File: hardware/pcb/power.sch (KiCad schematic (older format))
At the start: 15 parts

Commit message: schematic updates
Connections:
- net GND: no longer C?.2 (BATT-)
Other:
- moved on the sheet: C?, U?
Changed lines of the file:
@@
 L TPS783 U?
 U 1 1 552EDEA7
-P 5500 5700
-F 0 "U?" H 5350 5950 60  0000 C CNN
-F 1 "TPS783" H 5650 5450 60  0000 C CNN
-F 2 "" H 5350 5650 60  0000 C CNN
-F 3 "" H 5350 5650 60  0000 C CNN
-	1    5500 5700
-	1    0    0    -1
-$EndComp
-Text HLabel 6500 5600 2    60   Input ~ 0
+P 6500 4100
+F 0 "U?" H 6350 4350 60  0000 C CNN
+F 1 "TPS783" H 6650 3850 60  0000 C CNN
+F 2 "" H 6350 4050 60  0000 C CNN
+F 3 "" H 6350 4050 60  0000 C CNN
+	1    6500 4100
+	1    0    0    -1
+$EndComp
+Text HLabel 7500 3550 1    60   Input ~ 0
 +3V
 $Comp
 L GND #PWR035
 U 1 1 552EE044
-P 5500 6200
-F 0 "#PWR035" H 5500 5950 50  0001 C CNN
-F 1 "GND" H 5500 6050 50  0000 C CNN
-F 2 "" H 5500 6200 60  0000 C CNN
-F 3 "" H 5500 6200 60  0000 C CNN
-	1    5500 6200
+P 6500 4600
+F 0 "#PWR035" H 6500 4350 50  0001 C CNN
+F 1 "GND" H 6500 4450 50  0000 C CNN
+F 2 "" H 6500 4600 60  0000 C CNN
+F 3 "" H 6500 4600 60  0000 C CNN
+	1    6500 4600
 	1    0    0    -1
 $EndComp
@@
 L C C?
 U 1 1 552EE08E
-P 4850 5750
-F 0 "C?" H 4875 5850 50  0000 L CNN
-F 1 "C" H 4875 5650 50  0000 L CNN
-F 2 "" H 4888 5600 30  0000 C CNN
-F 3 "" H 4850 5750 60  0000 C CNN
-	1    4850 5750
+P 5850 4150
+F 0 "C?" H 5875 4250 50  0000 L CNN
+F 1 "C" H 5875 4050 50  0000 L CNN
+F 2 "" H 5888 4000 30  0000 C CNN
+F 3 "" H 5850 4150 60  0000 C CNN
+	1    5850 4150
 	1    0    0    -1
 $EndComp
@@
 L C C?
 U 1 1 552EE0AE
-P 6100 5750
-F 0 "C?" H 6125 5850 50  0000 L CNN
-F 1 "C" H 6125 5650 50  0000 L CNN
-F 2 "" H 6138 5600 30  0000 C CNN
-F 3 "" H 6100 5750 60  0000 C CNN
-	1    6100 5750
+P 7100 4150
+F 0 "C?" H 7125 4250 50  0000 L CNN
+F 1 "C" H 7125 4050 50  0000 L CNN
+F 2 "" H 7138 4000 30  0000 C CNN
+F 3 "" H 7100 4150 60  0000 C CNN
+	1    7100 4150
 	1    0    0    -1
 $EndComp
@@
 $EndComp
 Wire Wire Line
-	5500 6100 5500 6200
-Connection ~ 5500 6100
-Wire Wire Line
-	4850 5600 5050 5600
-Wire Wire Line
-	5050 5700 5000 5700
-Wire Wire Line
-	5000 5700 5000 6100
-Wire Wire Line
-	5000 6100 5900 6100
-Wire Wire Line
-	5900 5600 6500 5600
-Connection ~ 6100 5600
-Wire Wire Line
-	5900 6100 5900 5700
-Wire Wire Line
-	6100 5900 5900 5900
-Connection ~ 5900 5900
-Wire Wire Line
-	4850 5900 5000 5900
-Connection ~ 5000 5900
+	6500 4500 6500 4600
+Connection ~ 6500 4500
+Wire Wire Line
+	4050 4000 6050 4000
+Wire Wire Line
+	6050 4100 6000 4100
+Wire Wire Line
+	6000 4100 6000 4500
+Wire Wire Line
+	6000 4500 6900 4500
+Wire Wire Line
+	6900 4000 7500 4000
+Connection ~ 7100 4000
+Wire Wire Line
+	6900 4500 6900 4100
+Wire Wire Line
+	7100 4300 6900 4300
+Connection ~ 6900 4300
+Wire Wire Line
+	5850 4300 6000 4300
+Connection ~ 6000 4300
 Wire Wire Line
 	2350 2650 3050 2650
@@
 L LiPoly_Conn C?
 U 1 1 5530053E
-P 5750 4200
-F 0 "C?" H 5700 4600 60  0000 C CNN
-F 1 "LiPoly_Conn" H 5900 4100 60  0000 C CNN
-F 2 "" H 5750 4200 60  0000 C CNN
-F 3 "" H 5750 4200 60  0000 C CNN
-	1    5750 4200
-	1    0    0    -1
+P 5050 4550
+F 0 "C?" H 5000 4950 60  0000 C CNN
+F 1 "LiPoly_Conn" H 5200 4450 60  0000 C CNN
+F 2 "" H 5050 4550 60  0000 C CNN
+F 3 "" H 5050 4550 60  0000 C CNN
+	1    5050 4550
+	0    1    1    0
 $EndComp
 $Comp
@@
 	4050 4100 4100 4100
 $Comp
-L GND #PWR039
-U 1 1 553009E7
-P 5450 4600
-F 0 "#PWR039" H 5450 4350 50  0001 C CNN
-F 1 "GND" H 5450 4450 50  0000 C CNN
-F 2 "" H 5450 4600 60  0000 C CNN
-F 3 "" H 5450 4600 60  0000 C CNN
-	1    5450 4600
-	1    0    0    -1
-$EndComp
-Wire Wire Line
-	5450 4600 5450 4100
-Wire Wire Line
-	5450 4100 4400 4100
-Wire Wire Line
-	5550 4150 5450 4150
-Connection ~ 5450 4150
-Wire Wire Line
-	5550 4000 4050 4000
-$Comp
 L +VBATT P?
 U 1 1 55300EB5
-P 4950 3750
-F 0 "P?" H 5050 3750 60  0001 C CNN
-F 1 "+VBATT" H 4950 4050 60  0000 C CNN
-F 2 "" H 4950 3750 60  0000 C CNN
-F 3 "" H 4950 3750 60  0000 C CNN
-	1    4950 3750
-	1    0    0    -1
-$EndComp
-Wire Wire Line
-	4950 3750 4950 4000
-Connection ~ 4950 4000
-Wire Wire Line
-	4850 5600 4850 4000
+P 5550 3650
+F 0 "P?" H 5650 3650 60  0001 C CNN
+F 1 "+VBATT" H 5550 3950 60  0000 C CNN
+F 2 "" H 5550 3650 60  0000 C CNN
+F 3 "" H 5550 3650 60  0000 C CNN
+	1    5550 3650
+	1    0    0    -1
+$EndComp
 Connection ~ 4850 4000
 Text Notes 2950 4850 0    60   ~ 0
@@
 Wire Wire Line
 	4700 4200 4700 1800
+$Comp
+L GND #PWR?
+U 1 1 5539487A
+P 4550 4350
+F 0 "#PWR?" H 4550 4100 50  0001 C CNN
+F 1 "GND" H 4550 4200 50  0000 C CNN
+F 2 "" H 4550 4350 60  0000 C CNN
+F 3 "" H 4550 4350 60  0000 C CNN
+	1    4550 4350
+	1    0    0    -1
+$EndComp
+Wire Wire Line
+	4400 4100 4550 4100
+Wire Wire Line
+	4550 4100 4550 4350
+Wire Wire Line
+	5250 4350 5250 4000
+Connection ~ 5250 4000
+Wire Wire Line
+	5550 4000 5550 3650
+Connection ~ 5550 4000
+Connection ~ 5850 4000
+Wire Wire Line
+	7500 4000 7500 3550
 $EndSCHEMATC

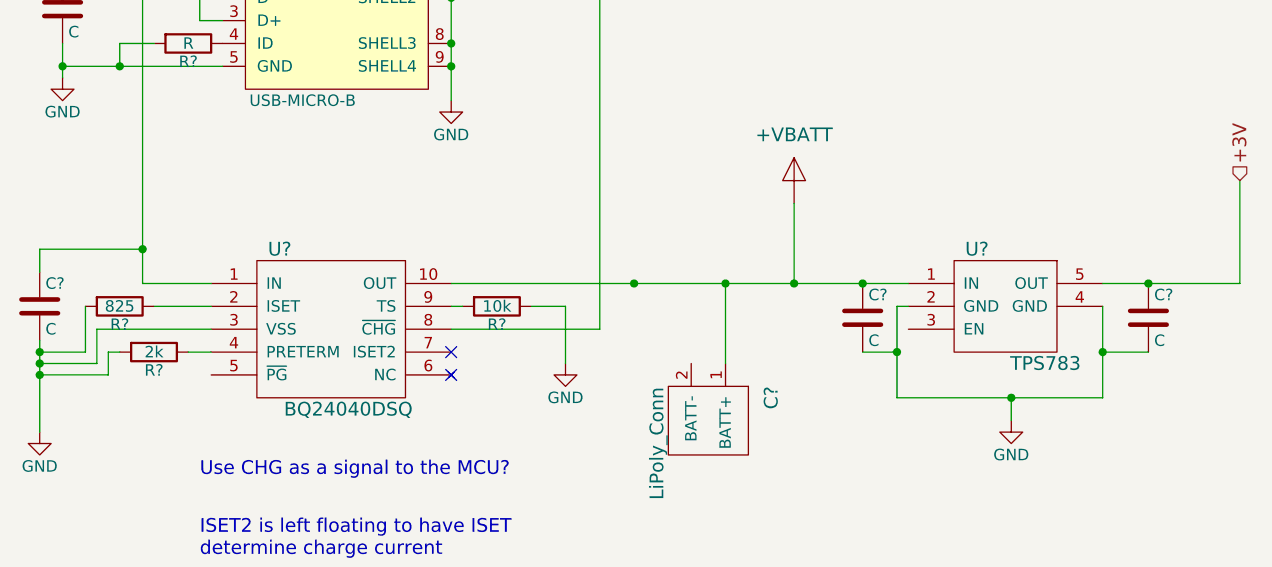
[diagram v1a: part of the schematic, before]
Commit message: Added component values
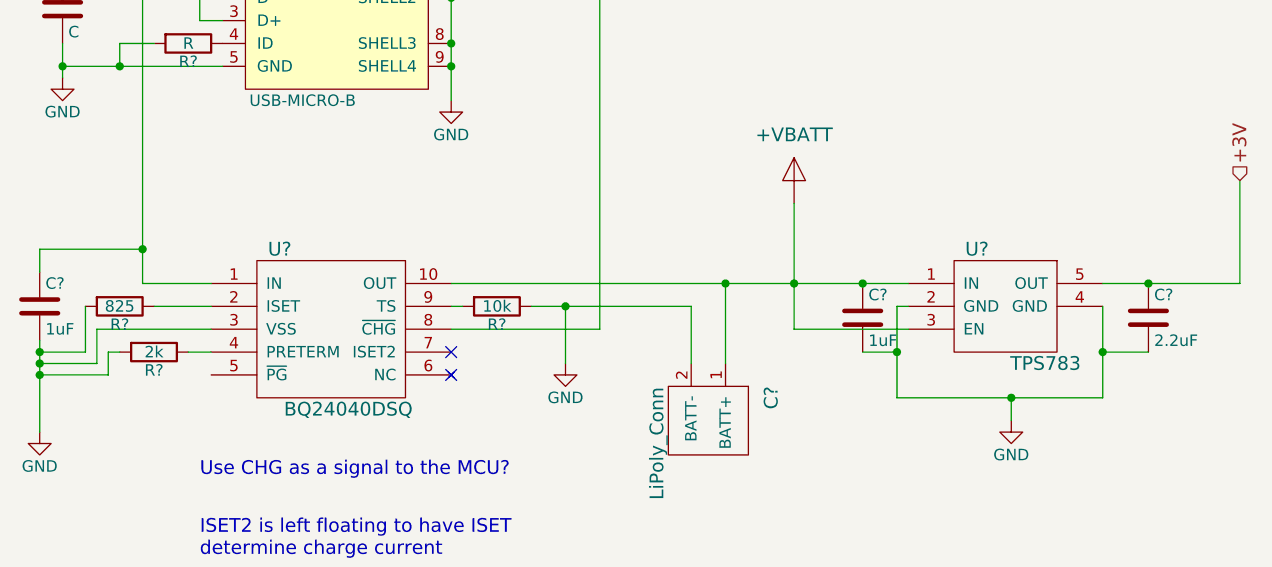
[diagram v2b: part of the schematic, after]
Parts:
- C? (x2): value C -> 1uF
- C?: value C -> 2.2uF
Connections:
- net GND: now also C?.2 (BATT-)
- net Vbatt: now also U?.3 (EN)
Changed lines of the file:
@@
 P 5850 4150
 F 0 "C?" H 5875 4250 50  0000 L CNN
-F 1 "C" H 5875 4050 50  0000 L CNN
+F 1 "1uF" H 5875 4050 50  0000 L CNN
 F 2 "" H 5888 4000 30  0000 C CNN
 F 3 "" H 5850 4150 60  0000 C CNN
@@
 P 7100 4150
 F 0 "C?" H 7125 4250 50  0000 L CNN
-F 1 "C" H 7125 4050 50  0000 L CNN
+F 1 "2.2uF" H 7125 4050 50  0000 L CNN
 F 2 "" H 7138 4000 30  0000 C CNN
 F 3 "" H 7100 4150 60  0000 C CNN
@@
 P 2250 4100
 F 0 "C?" H 2275 4200 50  0000 L CNN
-F 1 "C" H 2275 4000 50  0000 L CNN
+F 1 "1uF" H 2275 4000 50  0000 L CNN
 F 2 "" H 2288 3950 30  0000 C CNN
 F 3 "" H 2250 4100 60  0000 C CNN
@@
 	1    0    0    -1
 $EndComp
-Connection ~ 4850 4000
 Text Notes 2950 4850 0    60   ~ 0
 Use CHG as a signal to the MCU?
@@
 $EndComp
 Wire Wire Line
-	4400 4100 4550 4100
+	4400 4100 5100 4100
 Wire Wire Line
 	4550 4100 4550 4350
@@
 Connection ~ 5250 4000
 Wire Wire Line
-	5550 4000 5550 3650
+	5550 3650 5550 4200
 Connection ~ 5550 4000
 Connection ~ 5850 4000
 Wire Wire Line
 	7500 4000 7500 3550
+Wire Wire Line
+	5100 4100 5100 4350
+Connection ~ 4550 4100
+Wire Wire Line
+	5550 4200 6050 4200
 $EndSCHEMATC

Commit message: more changes
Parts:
- removed R?: R, symbol R
- gave numbers to parts that had none: 13
- renumbered 1uF to U8
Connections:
- net GND: now also CON1.4 (ID)
- net ~PG: now reaches U9.5 (~PG)

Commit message: mega commit
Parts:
- removed P1: +VBATT, symbol +VBATT
- added JP1, JP2: JUMPER, aero:Pin_Header_1x02, symbol JUMPER
- C28: renamed from C26; footprint (none) -> Capacitors_SMD:C_0603
- C29: renamed from U8; value C -> 1uF; footprint (none) -> Capacitors_SMD:C_0603
- C30: renamed from C28; footprint (none) -> Capacitors_SMD:C_0603
- C31: renamed from C29; footprint (none) -> Capacitors_SMD:C_0603
- CON1: footprint (none) -> aero:WM1399CT-ND
- J2: renamed from C27; footprint (none) -> Capacitors_SMD:C_1206_HandSoldering
- R10: renamed from R9; footprint (none) -> Resistors_SMD:R_0603
- R11: renamed from R10; footprint (none) -> Resistors_SMD:R_0603
- R7: renamed from R6; footprint (none) -> Resistors_SMD:R_0603
- R8: renamed from R7; footprint (none) -> Resistors_SMD:R_0603
- R9: renamed from R8; footprint (none) -> Resistors_SMD:R_0603
- U6: renamed from U9; footprint (none) -> aero:WSON-10-1EP
- U7: renamed from U10; footprint (none) -> Housings_SOT-23_SOT-143_TSOT-6:SOT-23-5
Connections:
- net Vbatt: now also JP2.1; no longer J2.1 (BATT+)
- net at C29.1, CON1.1 (VBUS): now also JP1.1; no longer C28.1, U6.1 (IN)
- new net: C28.1, JP1.2, U6.1 (IN)
- new net: J2.1 (BATT+), JP2.2
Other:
- moved on the sheet: C30, J2

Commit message: pre major restructuring commit
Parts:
- C25: renamed from C28; footprint Capacitors_SMD:C_0603 -> Capacitors_SMD:C_0402
- C26: renamed from C29; footprint Capacitors_SMD:C_0603 -> Capacitors_SMD:C_0402
- C27: renamed from C30; footprint Capacitors_SMD:C_0603 -> Capacitors_SMD:C_0402
- C28: renamed from C31; footprint Capacitors_SMD:C_0603 -> Capacitors_SMD:C_0402
- CON1: footprint aero:WM1399CT-ND -> (none)
- J2: footprint Capacitors_SMD:C_1206_HandSoldering -> (none)
- JP1, JP2: footprint aero:Pin_Header_1x02 -> (none)
- R10: renamed from R11; footprint Resistors_SMD:R_0603 -> Resistors_SMD:R_0402
- R6: renamed from R7; footprint Resistors_SMD:R_0603 -> Resistors_SMD:R_0402
- R7: renamed from R8; footprint Resistors_SMD:R_0603 -> Resistors_SMD:R_0402
- R8: renamed from R9; footprint Resistors_SMD:R_0603 -> Resistors_SMD:R_0402
- R9: renamed from R10; footprint Resistors_SMD:R_0603 -> Resistors_SMD:R_0402
- renumbered U6 to U7, U7 to U8
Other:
- note removed: "Use CHG as a signal to the MCU?"
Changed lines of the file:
@@
 $Descr A4 11693 8268
 encoding utf-8
-Sheet 6 7
+Sheet 6 8
 Title ""
 Date ""
@@
 $EndDescr
 $Comp
-L BQ24040DSQ U6
+L BQ24040DSQ U7
 U 1 1 552EDAA5
 P 3550 4400
-F 0 "U6" H 3300 4950 60  0000 C CNN
+F 0 "U7" H 3300 4950 60  0000 C CNN
 F 1 "BQ24040DSQ" H 3600 4250 60  0000 C CNN
 F 2 "aero:WSON-10-1EP" H 3400 4400 60  0001 C CNN
@@
 $EndComp
 $Comp
-L TPS783 U7
+L TPS783 U8
 U 1 1 552EDEA7
 P 6500 4100
-F 0 "U7" H 6350 4350 60  0000 C CNN
+F 0 "U8" H 6350 4350 60  0000 C CNN
 F 1 "TPS783" H 6650 3850 60  0000 C CNN
 F 2 "Housings_SOT-23_SOT-143_TSOT-6:SOT-23-5" H 6350 4050 60  0001 C CNN
@@
 +3V
 $Comp
-L GND #PWR043
+L GND #PWR039
 U 1 1 552EE044
 P 6500 4600
-F 0 "#PWR043" H 6500 4350 50  0001 C CNN
+F 0 "#PWR039" H 6500 4350 50  0001 C CNN
 F 1 "GND" H 6500 4450 50  0000 C CNN
 F 2 "" H 6500 4600 60  0000 C CNN
@@
 $EndComp
 $Comp
-L C C30
+L C C27
 U 1 1 552EE08E
 P 5750 4300
-F 0 "C30" H 5775 4400 50  0000 L CNN
+F 0 "C27" H 5775 4400 50  0000 L CNN
 F 1 "1uF" H 5775 4200 50  0000 L CNN
-F 2 "Capacitors_SMD:C_0603" H 5788 4150 30  0001 C CNN
+F 2 "Capacitors_SMD:C_0402" H 5788 4150 30  0001 C CNN
 F 3 "" H 5750 4300 60  0000 C CNN
 	1    5750 4300
@@
 $EndComp
 $Comp
-L C C31
+L C C28
 U 1 1 552EE0AE
 P 7100 4150
-F 0 "C31" H 7125 4250 50  0000 L CNN
+F 0 "C28" H 7125 4250 50  0000 L CNN
 F 1 "2.2uF" H 7125 4050 50  0000 L CNN
-F 2 "Capacitors_SMD:C_0603" H 7138 4000 30  0001 C CNN
+F 2 "Capacitors_SMD:C_0402" H 7138 4000 30  0001 C CNN
 F 3 "" H 7100 4150 60  0000 C CNN
 	1    7100 4150
@@
 $EndComp
 $Comp
-L C C29
+L C C26
 U 1 1 552EE372
 P 2350 2800
-F 0 "C29" H 2375 2900 50  0000 L CNN
+F 0 "C26" H 2375 2900 50  0000 L CNN
 F 1 "1uF" H 2375 2700 50  0000 L CNN
-F 2 "Capacitors_SMD:C_0603" H 2388 2650 30  0001 C CNN
+F 2 "Capacitors_SMD:C_0402" H 2388 2650 30  0001 C CNN
 F 3 "" H 2350 2800 60  0000 C CNN
 	1    2350 2800
@@
 $EndComp
 $Comp
-L GND #PWR044
+L GND #PWR040
 U 1 1 552EE3B1
 P 2350 3100
-F 0 "#PWR044" H 2350 2850 50  0001 C CNN
+F 0 "#PWR040" H 2350 2850 50  0001 C CNN
 F 1 "GND" H 2350 2950 50  0000 C CNN
 F 2 "" H 2350 3100 60  0000 C CNN
@@
 NoConn ~ 4050 4400
 $Comp
-L R R9
+L R R8
 U 1 1 552EFAB2
 P 2800 2150
-F 0 "R9" V 2880 2150 50  0000 C CNN
+F 0 "R8" V 2880 2150 50  0000 C CNN
 F 1 "22" V 2800 2150 50  0000 C CNN
-F 2 "Resistors_SMD:R_0603" V 2730 2150 30  0001 C CNN
+F 2 "Resistors_SMD:R_0402" V 2730 2150 30  0001 C CNN
 F 3 "" H 2800 2150 30  0000 C CNN
 	1    2800 2150
@@
 $EndComp
 $Comp
-L R R10
+L R R9
 U 1 1 552EFAE6
 P 2950 2150
-F 0 "R10" V 3030 2150 50  0000 C CNN
+F 0 "R9" V 3030 2150 50  0000 C CNN
 F 1 "22" V 2950 2150 50  0000 C CNN
-F 2 "Resistors_SMD:R_0603" V 2880 2150 30  0001 C CNN
+F 2 "Resistors_SMD:R_0402" V 2880 2150 30  0001 C CNN
 F 3 "" H 2950 2150 30  0000 C CNN
 	1    2950 2150
@@
 F 0 "CON1" H 3250 3200 50  0000 C CNN
 F 1 "USB-MICRO-B" H 3400 2500 50  0000 C CNN
-F 2 "aero:WM1399CT-ND" H 3550 2750 50  0001 C CNN
+F 2 "" H 3550 2750 50  0001 C CNN
 F 3 "" H 3550 2750 50  0000 C CNN
 	1    3550 2850
@@
 $EndComp
 $Comp
-L GND #PWR045
+L GND #PWR041
 U 1 1 552EFF3B
 P 4050 3200
-F 0 "#PWR045" H 4050 2950 50  0001 C CNN
+F 0 "#PWR041" H 4050 2950 50  0001 C CNN
 F 1 "GND" H 4050 3050 50  0000 C CNN
 F 2 "" H 4050 3200 60  0000 C CNN
@@
 $EndComp
 $Comp
-L C C28
+L C C25
 U 1 1 552F03A0
 P 2250 4100
-F 0 "C28" H 2275 4200 50  0000 L CNN
+F 0 "C25" H 2275 4200 50  0000 L CNN
 F 1 "1uF" H 2275 4000 50  0000 L CNN
-F 2 "Capacitors_SMD:C_0603" H 2288 3950 30  0001 C CNN
+F 2 "Capacitors_SMD:C_0402" H 2288 3950 30  0001 C CNN
 F 3 "" H 2250 4100 60  0000 C CNN
 	1    2250 4100
@@
 $EndComp
 $Comp
-L GND #PWR046
+L GND #PWR042
 U 1 1 552F03EA
 P 2250 4650
-F 0 "#PWR046" H 2250 4400 50  0001 C CNN
+F 0 "#PWR042" H 2250 4400 50  0001 C CNN
 F 1 "GND" H 2250 4500 50  0000 C CNN
 F 2 "" H 2250 4650 60  0000 C CNN
@@
 $EndComp
 $Comp
-L R R7
+L R R6
 U 1 1 553001BD
 P 2600 4100
-F 0 "R7" V 2680 4100 50  0000 C CNN
+F 0 "R6" V 2680 4100 50  0000 C CNN
 F 1 "825" V 2600 4100 50  0000 C CNN
-F 2 "Resistors_SMD:R_0603" V 2530 4100 30  0001 C CNN
+F 2 "Resistors_SMD:R_0402" V 2530 4100 30  0001 C CNN
 F 3 "" H 2600 4100 30  0000 C CNN
 	1    2600 4100
@@
 $EndComp
 $Comp
-L R R8
+L R R7
 U 1 1 553002D3
 P 2750 4300
-F 0 "R8" V 2830 4300 50  0000 C CNN
+F 0 "R7" V 2830 4300 50  0000 C CNN
 F 1 "2k" V 2750 4300 50  0000 C CNN
-F 2 "Resistors_SMD:R_0603" V 2680 4300 30  0001 C CNN
+F 2 "Resistors_SMD:R_0402" V 2680 4300 30  0001 C CNN
 F 3 "" H 2750 4300 30  0000 C CNN
 	1    2750 4300
@@
 F 0 "J2" H 5000 5900 60  0000 C CNN
 F 1 "LiPoly_Conn" H 5200 5400 60  0000 C CNN
-F 2 "Capacitors_SMD:C_1206_HandSoldering" H 5050 5500 60  0001 C CNN
+F 2 "" H 5050 5500 60  0001 C CNN
 F 3 "" H 5050 5500 60  0000 C CNN
 	1    5050 5500
@@
 $EndComp
 $Comp
-L R R11
+L R R10
 U 1 1 553008B3
 P 4250 4100
-F 0 "R11" V 4330 4100 50  0000 C CNN
+F 0 "R10" V 4330 4100 50  0000 C CNN
 F 1 "10k" V 4250 4100 50  0000 C CNN
-F 2 "Resistors_SMD:R_0603" V 4180 4100 30  0001 C CNN
+F 2 "Resistors_SMD:R_0402" V 4180 4100 30  0001 C CNN
 F 3 "" H 4250 4100 30  0000 C CNN
 	1    4250 4100
@@
 $EndComp
 $Comp
-L +VBATT #PWR047
+L +VBATT #PWR043
 U 1 1 55300EB5
 P 5550 3650
-F 0 "#PWR047" H 5650 3650 60  0001 C CNN
+F 0 "#PWR043" H 5650 3650 60  0001 C CNN
 F 1 "+VBATT" H 5550 3950 60  0000 C CNN
 F 2 "" H 5550 3650 60  0001 C CNN
@@
 	1    0    0    -1
 $EndComp
-Text Notes 2950 4850 0    60   ~ 0
-Use CHG as a signal to the MCU?
 NoConn ~ 4050 4300
 Text Notes 2950 5200 0    60   ~ 0
@@
 ~CHG
 $Comp
-L GND #PWR048
+L GND #PWR044
 U 1 1 5539487A
 P 4550 4350
-F 0 "#PWR048" H 4550 4100 50  0001 C CNN
+F 0 "#PWR044" H 4550 4100 50  0001 C CNN
 F 1 "GND" H 4550 4200 50  0000 C CNN
 F 2 "" H 4550 4350 60  0000 C CNN
@@
 ~PG
 $Comp
-L GND #PWR049
+L GND #PWR045
 U 1 1 5540EAF2
 P 4800 5150
-F 0 "#PWR049" H 4800 4900 50  0001 C CNN
+F 0 "#PWR045" H 4800 4900 50  0001 C CNN
 F 1 "GND" H 4800 5000 50  0000 C CNN
 F 2 "" H 4800 5150 60  0000 C CNN
@@
 $EndComp
 $Comp
-L PWR_FLAG #FLG050
+L PWR_FLAG #FLG046
 U 1 1 554024B4
 P 2350 2450
-F 0 "#FLG050" H 2350 2545 50  0001 C CNN
+F 0 "#FLG046" H 2350 2545 50  0001 C CNN
 F 1 "PWR_FLAG" H 2350 2630 50  0000 C CNN
 F 2 "" H 2350 2450 60  0000 C CNN
@@
 	1    2350 2450
 	1    0    0    -1
-$EndComp
-$Comp
-L PWR_FLAG #FLG051
-U 1 1 55405AAC
-P 2200 3050
-F 0 "#FLG051" H 2200 3145 50  0001 C CNN
-F 1 "PWR_FLAG" H 2200 3230 50  0000 C CNN
-F 2 "" H 2200 3050 60  0000 C CNN
-F 3 "" H 2200 3050 60  0000 C CNN
-	1    2200 3050
-	0    -1   -1   0
 $EndComp
 $Comp
@@
 F 0 "JP1" H 2700 3600 50  0000 C CNN
 F 1 "JUMPER" H 2700 3370 50  0000 C CNN
-F 2 "aero:Pin_Header_1x02" H 2700 3450 60  0001 C CNN
+F 2 "" H 2700 3450 60  0001 C CNN
 F 3 "" H 2700 3450 60  0000 C CNN
 	1    2700 3450
@@
 F 0 "JP2" H 5250 4950 50  0000 C CNN
 F 1 "JUMPER" H 5250 4720 50  0000 C CNN
-F 2 "aero:Pin_Header_1x02" H 5250 4800 60  0001 C CNN
+F 2 "" H 5250 4800 60  0001 C CNN
 F 3 "" H 5250 4800 60  0000 C CNN
 	1    5250 4800
@@
 Connection ~ 2350 3050
 Wire Wire Line
-	2200 3050 3050 3050
-Wire Wire Line
 	2950 2850 3050 2850
 Wire Wire Line
@@
 	6500 4500 6500 4600
 $Comp
-L PWR_FLAG #FLG052
+L PWR_FLAG #FLG047
 U 1 1 5543E6E0
 P 2900 3900
-F 0 "#FLG052" H 2900 3995 50  0001 C CNN
+F 0 "#FLG047" H 2900 3995 50  0001 C CNN
 F 1 "PWR_FLAG" H 2900 4080 50  0000 C CNN
 F 2 "" H 2900 3900 60  0000 C CNN
@@
 	5750 4450 5750 4500
 Connection ~ 6000 4500
+Wire Wire Line
+	2300 3050 3050 3050
+$Comp
+L PWR_FLAG #FLG048
+U 1 1 55B1C317
+P 2300 3050
+F 0 "#FLG048" H 2300 3145 50  0001 C CNN
+F 1 "PWR_FLAG" H 2300 3230 50  0000 C CNN
+F 2 "" H 2300 3050 60  0000 C CNN
+F 3 "" H 2300 3050 60  0000 C CNN
+	1    2300 3050
+	0    -1   -1   0
+$EndComp
 $EndSCHEMATC

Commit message: committing before shit starts breaking (pcbnew)
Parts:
- CON1: footprint (none) -> aero:WM1399CT-ND
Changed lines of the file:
@@
 F 0 "CON1" H 3250 3200 50  0000 C CNN
 F 1 "USB-MICRO-B" H 3400 2500 50  0000 C CNN
-F 2 "" H 3550 2750 50  0001 C CNN
+F 2 "aero:WM1399CT-ND" H 3550 2750 50  0001 C CNN
 F 3 "" H 3550 2750 50  0000 C CNN
 	1    3550 2850
@@
 	0    -1   -1   0
 $EndComp
+Text Label 5150 5800 0    60   ~ 0
+http://www.molex.com/molex/products/datasheet.jsp?part=active/0781710002_PCB_HEADERS.xml#partdetail
 $EndSCHEMATC

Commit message: more progress on new layout
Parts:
- J2: footprint (none) -> aero:Conn_Molex_78171-02
- JP1, JP2: footprint (none) -> aero:Pin_Header_1x02_2mm
- renumbered C25 to C23, C26 to C24, C27 to C25, C28 to C26, R6 to R5, R7 to R6, R8 to R7, R9 to R8, R10 to R9
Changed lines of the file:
@@
 $EndComp
 $Comp
-L C C27
+L C C25
 U 1 1 552EE08E
 P 5750 4300
-F 0 "C27" H 5775 4400 50  0000 L CNN
+F 0 "C25" H 5775 4400 50  0000 L CNN
 F 1 "1uF" H 5775 4200 50  0000 L CNN
 F 2 "Capacitors_SMD:C_0402" H 5788 4150 30  0001 C CNN
@@
 $EndComp
 $Comp
-L C C28
+L C C26
 U 1 1 552EE0AE
 P 7100 4150
-F 0 "C28" H 7125 4250 50  0000 L CNN
+F 0 "C26" H 7125 4250 50  0000 L CNN
 F 1 "2.2uF" H 7125 4050 50  0000 L CNN
 F 2 "Capacitors_SMD:C_0402" H 7138 4000 30  0001 C CNN
@@
 $EndComp
 $Comp
-L C C26
+L C C24
 U 1 1 552EE372
 P 2350 2800
-F 0 "C26" H 2375 2900 50  0000 L CNN
+F 0 "C24" H 2375 2900 50  0000 L CNN
 F 1 "1uF" H 2375 2700 50  0000 L CNN
 F 2 "Capacitors_SMD:C_0402" H 2388 2650 30  0001 C CNN
@@
 NoConn ~ 4050 4400
 $Comp
-L R R8
+L R R7
 U 1 1 552EFAB2
 P 2800 2150
-F 0 "R8" V 2880 2150 50  0000 C CNN
+F 0 "R7" V 2880 2150 50  0000 C CNN
 F 1 "22" V 2800 2150 50  0000 C CNN
 F 2 "Resistors_SMD:R_0402" V 2730 2150 30  0001 C CNN
@@
 $EndComp
 $Comp
-L R R9
+L R R8
 U 1 1 552EFAE6
 P 2950 2150
-F 0 "R9" V 3030 2150 50  0000 C CNN
+F 0 "R8" V 3030 2150 50  0000 C CNN
 F 1 "22" V 2950 2150 50  0000 C CNN
 F 2 "Resistors_SMD:R_0402" V 2880 2150 30  0001 C CNN
@@
 $EndComp
 $Comp
-L C C25
+L C C23
 U 1 1 552F03A0
 P 2250 4100
-F 0 "C25" H 2275 4200 50  0000 L CNN
+F 0 "C23" H 2275 4200 50  0000 L CNN
 F 1 "1uF" H 2275 4000 50  0000 L CNN
 F 2 "Capacitors_SMD:C_0402" H 2288 3950 30  0001 C CNN
@@
 $EndComp
 $Comp
-L R R6
+L R R5
 U 1 1 553001BD
 P 2600 4100
-F 0 "R6" V 2680 4100 50  0000 C CNN
+F 0 "R5" V 2680 4100 50  0000 C CNN
 F 1 "825" V 2600 4100 50  0000 C CNN
 F 2 "Resistors_SMD:R_0402" V 2530 4100 30  0001 C CNN
@@
 $EndComp
 $Comp
-L R R7
+L R R6
 U 1 1 553002D3
 P 2750 4300
-F 0 "R7" V 2830 4300 50  0000 C CNN
+F 0 "R6" V 2830 4300 50  0000 C CNN
 F 1 "2k" V 2750 4300 50  0000 C CNN
 F 2 "Resistors_SMD:R_0402" V 2680 4300 30  0001 C CNN
@@
 F 0 "J2" H 5000 5900 60  0000 C CNN
 F 1 "LiPoly_Conn" H 5200 5400 60  0000 C CNN
-F 2 "" H 5050 5500 60  0001 C CNN
+F 2 "aero:Conn_Molex_78171-02" H 5050 5500 60  0001 C CNN
 F 3 "" H 5050 5500 60  0000 C CNN
 	1    5050 5500
@@
 $EndComp
 $Comp
-L R R10
+L R R9
 U 1 1 553008B3
 P 4250 4100
-F 0 "R10" V 4330 4100 50  0000 C CNN
+F 0 "R9" V 4330 4100 50  0000 C CNN
 F 1 "10k" V 4250 4100 50  0000 C CNN
 F 2 "Resistors_SMD:R_0402" V 4180 4100 30  0001 C CNN
@@
 F 0 "JP1" H 2700 3600 50  0000 C CNN
 F 1 "JUMPER" H 2700 3370 50  0000 C CNN
-F 2 "" H 2700 3450 60  0001 C CNN
+F 2 "aero:Pin_Header_1x02_2mm" H 2700 3450 60  0001 C CNN
 F 3 "" H 2700 3450 60  0000 C CNN
 	1    2700 3450
@@
 F 0 "JP2" H 5250 4950 50  0000 C CNN
 F 1 "JUMPER" H 5250 4720 50  0000 C CNN
-F 2 "" H 5250 4800 60  0001 C CNN
+F 2 "aero:Pin_Header_1x02_2mm" H 5250 4800 60  0001 C CNN
 F 3 "" H 5250 4800 60  0000 C CNN
 	1    5250 4800
